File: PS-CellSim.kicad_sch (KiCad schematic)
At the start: 54 parts, among them J1 Conn_01x07, J2 Conn_01x01, J3 Conn_01x01, J4 Conn_01x02, J5 Conn_01x08

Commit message: swapped to jumpers for leds
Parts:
- added JP10, JP11, JP12, JP13, JP14, JP15, JP16, JP9: Jumper, symbol Jumper:Jumper_2_Small_Open
- R10, R12, R14, R16, R18, R20, R22, R24: now fitted
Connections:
- net GPIO1: now also JP9.2 (B); no longer R10.2
- net GPIO2: now also JP10.2 (B); no longer R12.2
- net GPIO3: now also JP11.2 (B); no longer R14.2
- net GPIO4: now also JP12.2 (B); no longer R16.2
- net GPIO5: now also JP13.2 (B); no longer R18.2
- net GPIO6: now also JP14.2 (B); no longer R20.2
- net GPIO7: now also JP15.2 (B); no longer R22.2
- net GPIO8: now also JP16.2 (B); no longer R24.2
- new net: JP13.1 (A), R18.2
- new net: JP10.1 (A), R12.2
- new net: JP9.1 (A), R10.2
- new net: JP16.1 (A), R24.2
- new net: JP15.1 (A), R22.2
- new net: JP12.1 (A), R16.2
- new net: JP14.1 (A), R20.2
- new net: JP11.1 (A), R14.2
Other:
- moved on the sheet: D1

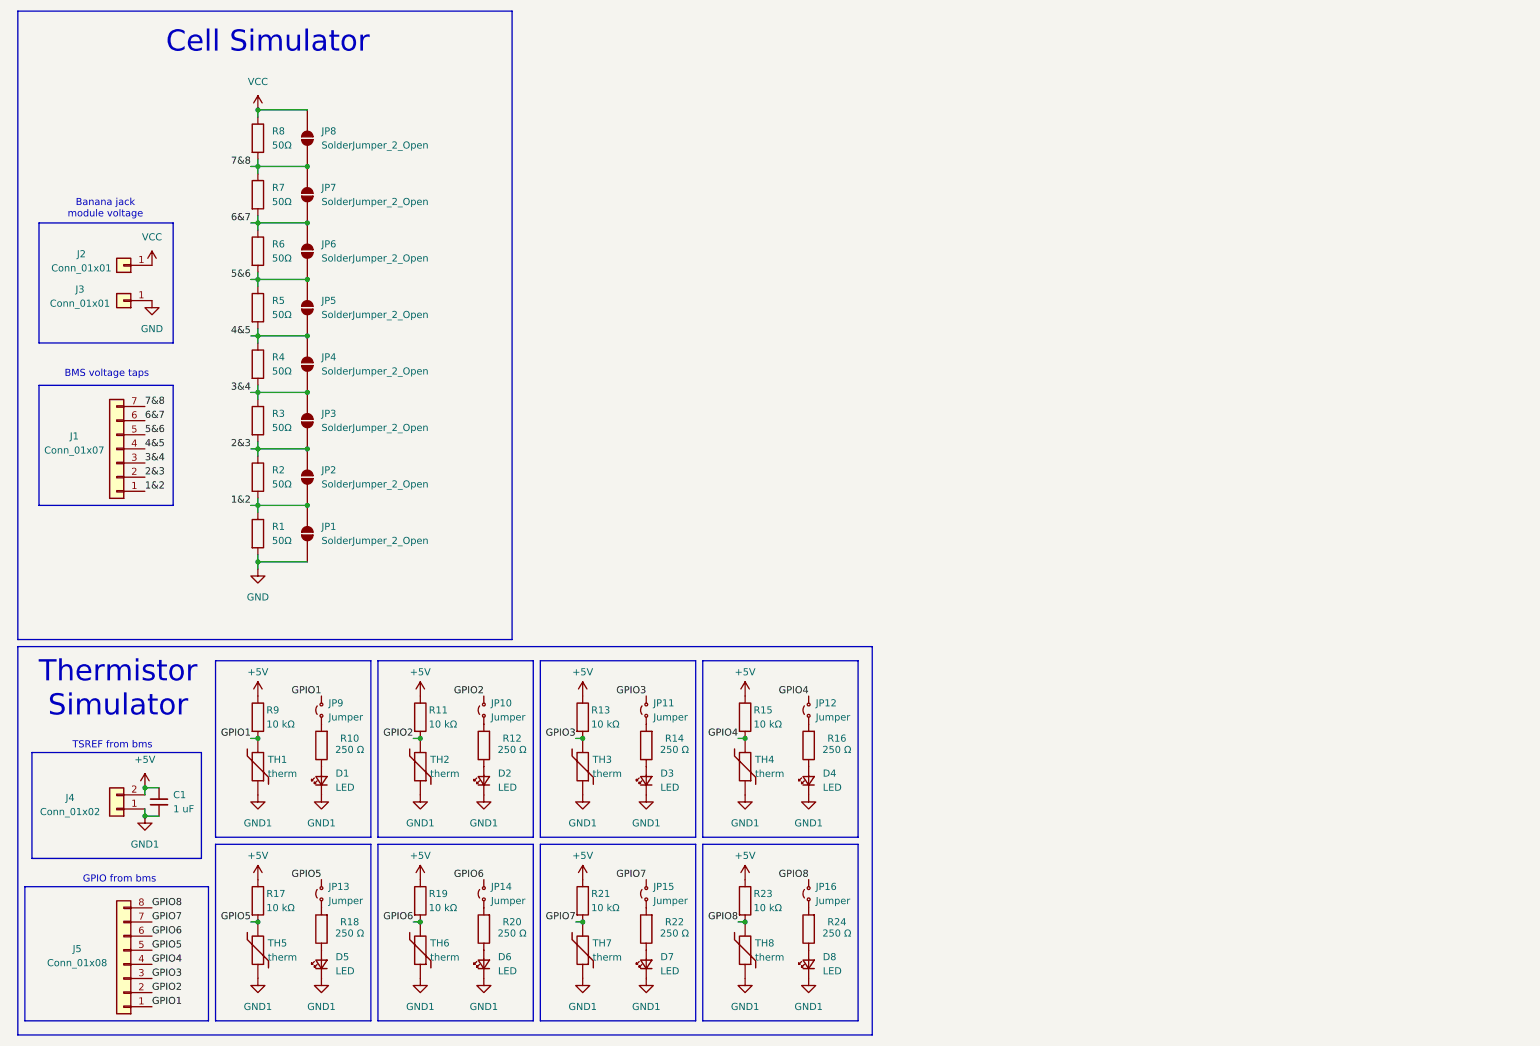
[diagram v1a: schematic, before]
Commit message: i added footprints, also thermistors now lead to nanofits
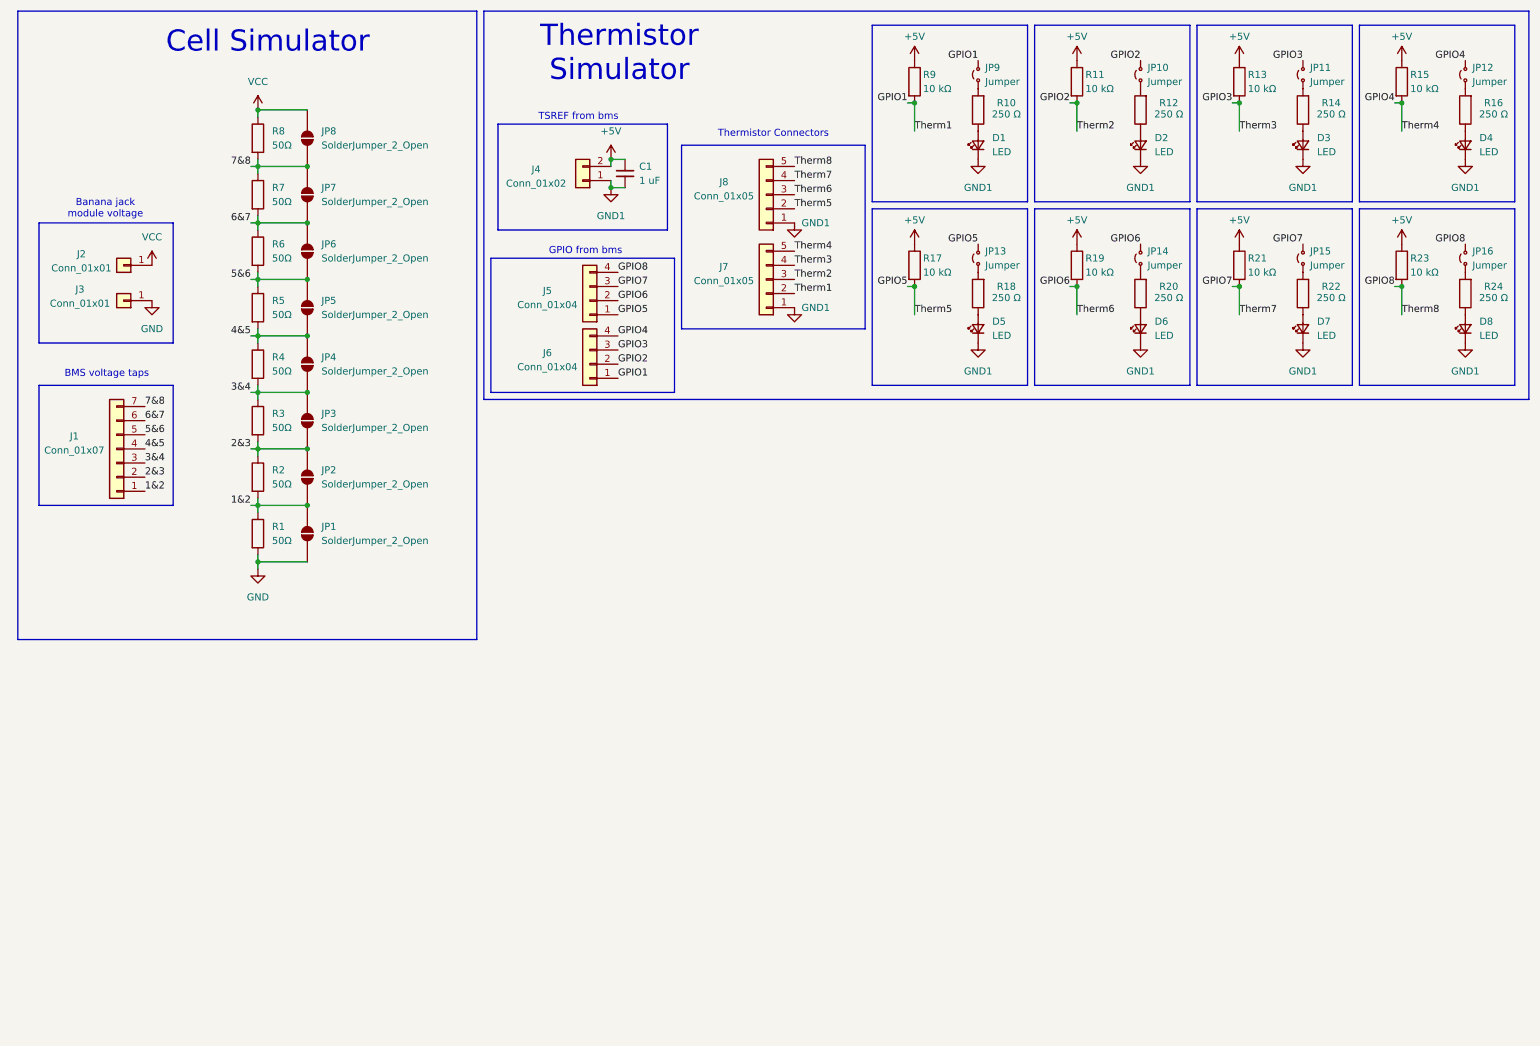
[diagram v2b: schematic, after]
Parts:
- removed J5: Conn_01x08, symbol Connector_Generic:Conn_01x08
- removed TH1, TH2, TH3, TH4, TH5, TH6, TH7, TH8: therm, symbol Device:Thermistor
- added J5, J6: Conn_01x04, UTSVT_Connectors:Molex_Nano-Fit_105313-xx04_1x04_P2.50mm_Horizontal, symbol Connector_Generic:Conn_01x04
- added J7, J8: Conn_01x05, UTSVT_Connectors:Molex_Nano-Fit_105313-xx05_1x05_P2.50mm_Horizontal, symbol Connector_Generic:Conn_01x05
- C1: footprint (none) -> Capacitor_SMD:C_0201_0603Metric
- D1, D2, D3, D4, D5, D6, D7, D8: footprint (none) -> LED_SMD:LED_0201_0603Metric
- J1: footprint (none) -> UTSVT_Connectors:Molex_Nano-Fit_105313-xx07_1x07_P2.50mm_Horizontal
- J2, J3: footprint (none) -> UTSVT_Connectors:Banana_Jack_1_Pin_4mm
- J4: footprint (none) -> UTSVT_Connectors:Molex_Nano-Fit_105313-xx02_1x02_P2.50mm_Horizontal
- JP1, JP2, JP3, JP4, JP5, JP6, JP7, JP8: footprint (none) -> Jumper:SolderJumper-2_P1.3mm_Open_TrianglePad1.0x1.5mm
- JP10, JP11, JP12, JP13, JP14, JP15, JP16, JP9: footprint (none) -> Connector_PinHeader_2.00mm:PinHeader_1x02_P2.00mm_Vertical
- R1, R10, R11, R12, R13, R14, R15, R16, R17, R18, R19, R2, R20, R21, R22, R23, R24, R3, R4, R5, R6, R7, R8, R9: footprint (none) -> Resistor_SMD:R_0603_1608Metric
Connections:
- net GND1: now also J7.1 (Pin_1), J8.1 (Pin_1)
- net GPIO1: now also J6.1 (Pin_1), J7.2 (Pin_2)
- net GPIO2: now also J6.2 (Pin_2), J7.3 (Pin_3)
- net GPIO3: now also J6.3 (Pin_3), J7.4 (Pin_4)
- net GPIO4: now also J6.4 (Pin_4), J7.5 (Pin_5)
- net GPIO5: now also J5.1 (Pin_1), J8.2 (Pin_2)
- net GPIO6: now also J5.2 (Pin_2), J8.3 (Pin_3)
- net GPIO7: now also J5.3 (Pin_3), J8.4 (Pin_4)
- net GPIO8: now also J5.4 (Pin_4), J8.5 (Pin_5)
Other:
- note added: "Thermistor Connectors"
- moved on the sheet: C1, D1, D2, D3, D4, D5, D6, D7, D8, J4, JP10, JP11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

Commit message: prelim layout made
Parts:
- C1: footprint Capacitor_SMD:C_0201_0603Metric -> Capacitor_SMD:C_0603_1608Metric
- D1, D2, D3, D4, D5, D6, D7, D8: footprint LED_SMD:LED_0201_0603Metric -> LED_SMD:LED_0603_1608Metric
- J1: value Conn_01x07 -> bms_taps
- J2: value Conn_01x01 -> bench_vcc
- J3: value Conn_01x01 -> bench_gnd
- J4: value Conn_01x02 -> bms_ref
- J5: value Conn_01x04 -> bms_gpio_set2
- J6: value Conn_01x04 -> bms_gpio_set1
- J7: value Conn_01x05 -> therm_set1
- J8: value Conn_01x05 -> therm_set2
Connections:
- net GPIO1: now also J7.5 (Pin_5); no longer J7.2 (Pin_2)
- net GPIO2: now also J7.4 (Pin_4); no longer J7.3 (Pin_3)
- net GPIO3: now also J7.3 (Pin_3); no longer J7.4 (Pin_4)
- net GPIO4: now also J7.2 (Pin_2); no longer J7.5 (Pin_5)
- net GPIO5: now also J8.5 (Pin_5); no longer J8.2 (Pin_2)
- net GPIO6: now also J8.4 (Pin_4); no longer J8.3 (Pin_3)
- net GPIO7: now also J8.3 (Pin_3); no longer J8.4 (Pin_4)
- net GPIO8: now also J8.2 (Pin_2); no longer J8.5 (Pin_5)
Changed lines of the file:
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@@
 		)
 	)
-	(label "Therm1"
-		(at 152.4 63.5 0)
-		(effects
-			(font
-				(size 1.27 1.27)
-			)
-			(justify left bottom)
-		)
-	)
 	(label "7&8"
 		(at 35.56 83.82 0)
@@
 		)
 	)
-	(label "Therm5"
-		(at 152.4 48.26 0)
+	(label "Therm2"
+		(at 152.4 58.42 0)
 		(effects
 			(font
@@
 		)
 	)
-	(label "Therm4"
-		(at 152.4 55.88 0)
-		(effects
-			(font
-				(size 1.27 1.27)
-			)
-			(justify left bottom)
-		)
-	)
-	(label "Therm3"
-		(at 152.4 58.42 0)
+	(label "Therm6"
+		(at 152.4 43.18 0)
 		(effects
 			(font
@@
 		)
 	)
+	(label "Therm7"
+		(at 152.4 45.72 0)
+		(effects
+			(font
+				(size 1.27 1.27)
+			)
+			(justify left bottom)
+		)
+	)
 	(label "GPIO2"
 		(at 214.63 21.59 180)
@@
 		)
 	)
+	(label "Therm8"
+		(at 152.4 48.26 0)
+		(effects
+			(font
+				(size 1.27 1.27)
+			)
+			(justify left bottom)
+		)
+	)
 	(label "GPIO5"
 		(at 185.42 54.61 180)
@@
 		)
 	)
-	(label "Therm2"
+	(label "Therm3"
 		(at 152.4 60.96 0)
 		(effects
@@
 		)
 	)
-	(label "Therm8"
-		(at 152.4 40.64 0)
-		(effects
-			(font
-				(size 1.27 1.27)
-			)
-			(justify left bottom)
-		)
-	)
 	(label "GPIO1"
 		(at 172.72 29.21 180)
@@
 		)
 	)
-	(label "3&4"
-		(at 35.56 93.98 0)
+	(label "Therm1"
+		(at 152.4 55.88 0)
 		(effects
 			(font
@@
 		)
 	)
-	(label "GPIO8"
-		(at 120.65 59.69 0)
+	(label "3&4"
+		(at 35.56 93.98 0)
 		(effects
 			(font
@@
 		)
 	)
-	(label "Therm7"
-		(at 152.4 43.18 0)
+	(label "GPIO8"
+		(at 120.65 59.69 0)
 		(effects
 			(font
@@
 		)
 	)
+	(label "Therm5"
+		(at 152.4 40.64 0)
+		(effects
+			(font
+				(size 1.27 1.27)
+			)
+			(justify left bottom)
+		)
+	)
 	(label "Therm3"
 		(at 232.41 34.29 0)
@@
 		)
 	)
-	(label "GPIO7"
-		(at 243.84 54.61 180)
+	(label "Therm4"
+		(at 152.4 63.5 0)
 		(effects
 			(font
 				(size 1.27 1.27)
 			)
-			(justify right bottom)
+			(justify left bottom)
 		)
 	)
-	(label "Therm6"
-		(at 152.4 45.72 0)
+	(label "GPIO7"
+		(at 243.84 54.61 180)
 		(effects
 			(font
 				(size 1.27 1.27)
 			)
-			(justify left bottom)
+			(justify right bottom)
 		)
 	)
@@
 			)
 		)
-		(property "Value" "Conn_01x01"
+		(property "Value" "bench_gnd"
 			(at 23.876 65.278 0)
 			(show_name no)
@@
 			)
 		)
-		(property "Footprint" "LED_SMD:LED_0201_0603Metric"
+		(property "Footprint" "LED_SMD:LED_0603_1608Metric"
 			(at 214.63 69.85 90)
 			(hide yes)
@@
 		(dnp no)
 		(property "Reference" "J5"
-			(at 107.95 62.992 0)
+			(at 106.172 62.992 0)
 			(show_name no)
 			(do_not_autoplace no)
@@
 			)
 		)
-		(property "Value" "Conn_01x04"
-			(at 107.95 65.532 0)
+		(property "Value" "bms_gpio_set2"
+			(at 106.172 65.532 0)
 			(show_name no)
 			(do_not_autoplace no)
@@
 			)
 		)
-		(property "Value" "Conn_01x05"
+		(property "Value" "therm_set2"
 			(at 139.7 45.974 0)
 			(show_name no)
@@
 			)
 		)
-		(property "Value" "Conn_01x02"
+		(property "Value" "bms_ref"
 			(at 105.918 43.688 0)
 			(show_name no)
@@
 			)
 		)
-		(property "Footprint" "LED_SMD:LED_0201_0603Metric"
+		(property "Footprint" "LED_SMD:LED_0603_1608Metric"
 			(at 273.05 69.85 90)
 			(hide yes)
@@
 			)
 		)
-		(property "Footprint" "LED_SMD:LED_0201_0603Metric"
+		(property "Footprint" "LED_SMD:LED_0603_1608Metric"
 			(at 243.84 36.83 90)
 			(hide yes)
@@
 			)
 		)
-		(property "Value" "Conn_01x01"
+		(property "Value" "bench_vcc"
 			(at 24.13 58.928 0)
 			(show_name no)
@@
 			)
 		)
-		(property "Footprint" "Capacitor_SMD:C_0201_0603Metric"
+		(property "Footprint" "Capacitor_SMD:C_0603_1608Metric"
 			(at 121.92 41.91 0)
 			(hide yes)
@@
 			)
 		)
-		(property "Footprint" "LED_SMD:LED_0201_0603Metric"
+		(property "Footprint" "LED_SMD:LED_0603_1608Metric"
 			(at 243.84 69.85 90)
 			(hide yes)
@@
 			)
 		)
-		(property "Footprint" "LED_SMD:LED_0201_0603Metric"
+		(property "Footprint" "LED_SMD:LED_0603_1608Metric"
 			(at 185.42 69.85 90)
 			(hide yes)
@@
 			)
 		)
-		(property "Value" "Conn_01x05"
+		(property "Value" "therm_set1"
 			(at 139.7 61.214 0)
 			(show_name no)
@@
 			)
 		)
-		(property "Value" "Conn_01x07"
+		(property "Value" "bms_taps"
 			(at 22.86 91.694 0)
 			(show_name no)
@@
 		(dnp no)
 		(property "Reference" "J6"
-			(at 107.95 74.168 0)
+			(at 106.172 74.168 0)
 			(show_name no)
 			(do_not_autoplace no)
@@
 			)
 		)
-		(property "Value" "Conn_01x04"
-			(at 107.95 76.708 0)
+		(property "Value" "bms_gpio_set1"
+			(at 106.172 76.708 0)
 			(show_name no)
 			(do_not_autoplace no)
@@
 			)
 		)
-		(property "Footprint" "LED_SMD:LED_0201_0603Metric"
+		(property "Footprint" "LED_SMD:LED_0603_1608Metric"
 			(at 185.42 36.83 90)
 			(hide yes)
@@
 			)
 		)
-		(property "Footprint" "LED_SMD:LED_0201_0603Metric"
+		(property "Footprint" "LED_SMD:LED_0603_1608Metric"
 			(at 273.05 36.83 90)
 			(hide yes)
@@
 			)
 		)
-		(property "Footprint" "LED_SMD:LED_0201_0603Metric"
+		(property "Footprint" "LED_SMD:LED_0603_1608Metric"
 			(at 214.63 36.83 90)
 			(hide yes)
